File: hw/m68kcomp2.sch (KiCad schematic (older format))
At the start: 1 part

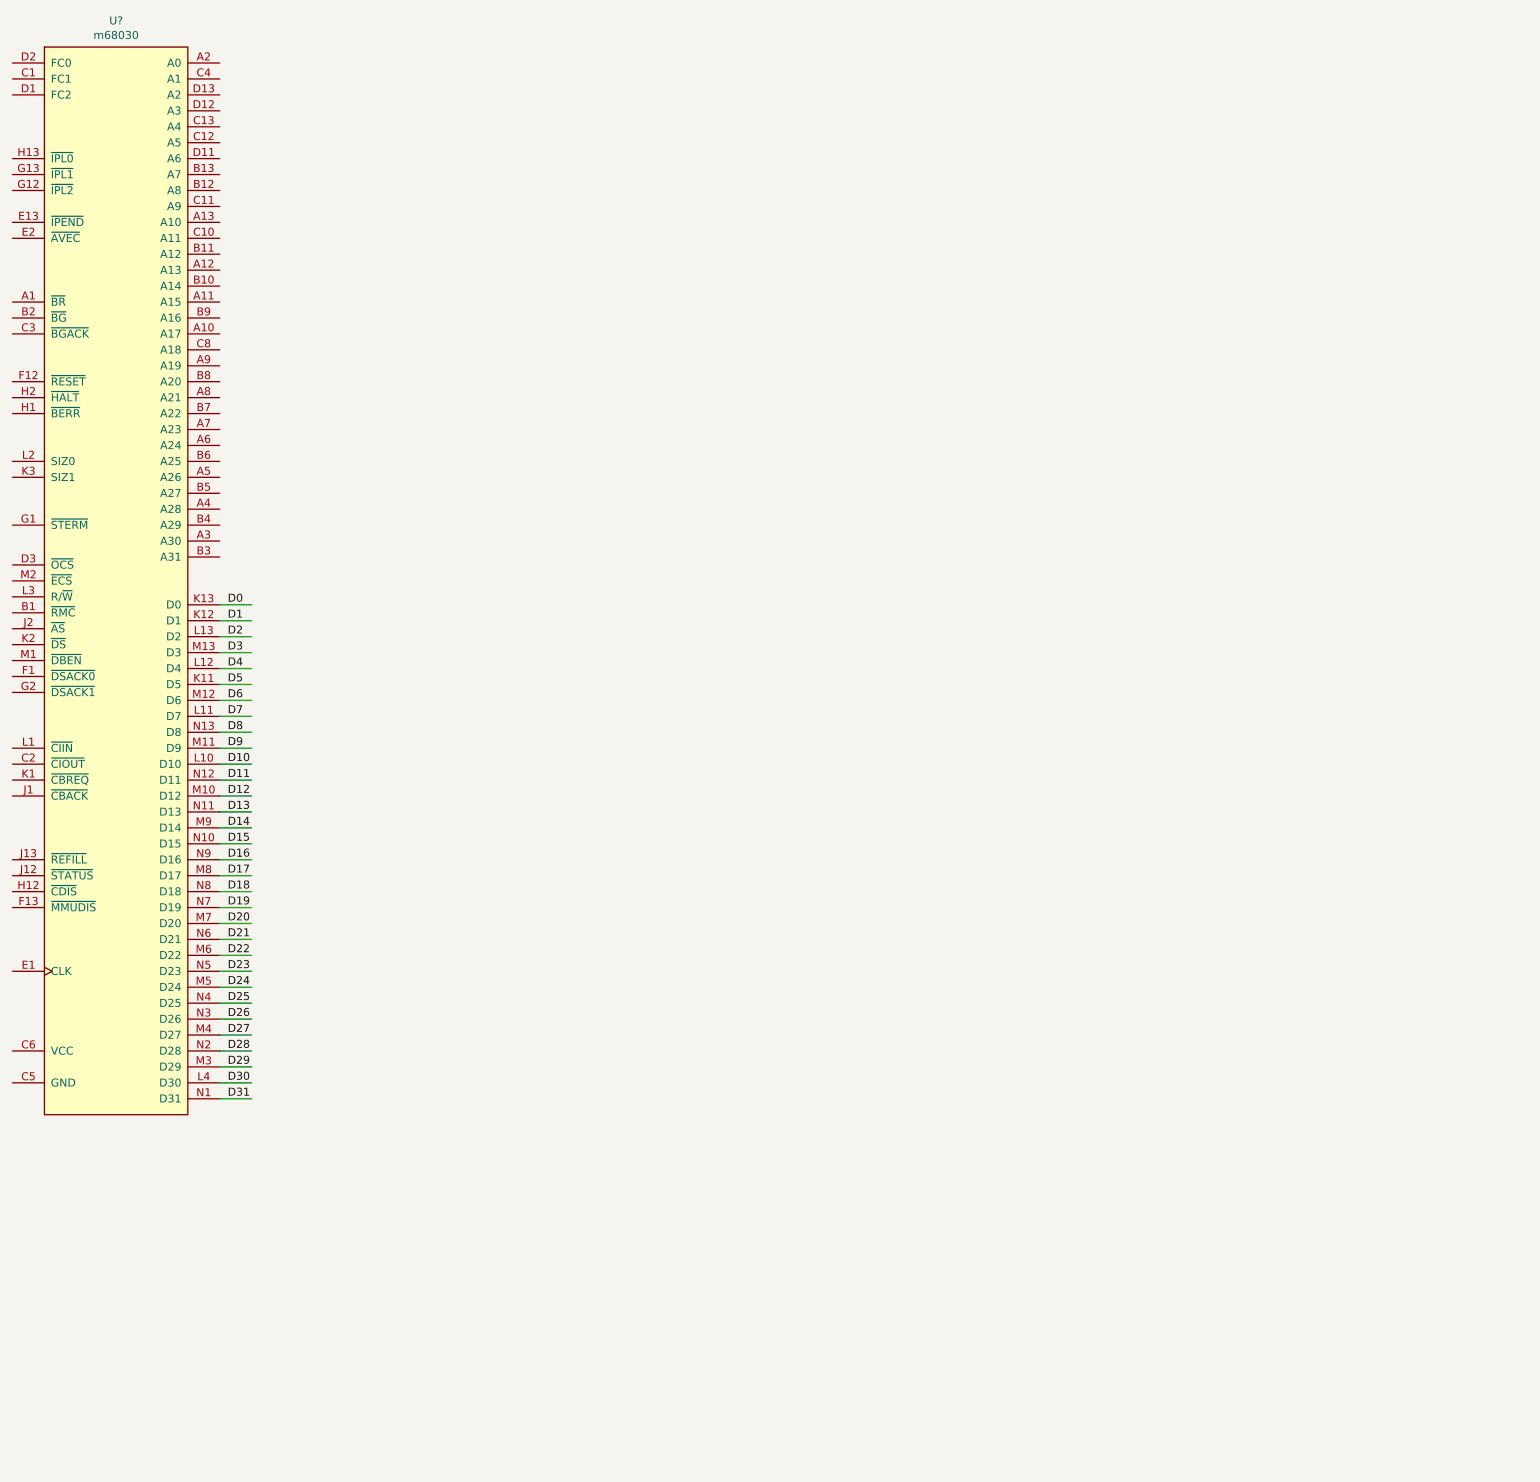
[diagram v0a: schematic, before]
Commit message: finished the 68881 symbol, and added a few major components on a schematic sheet
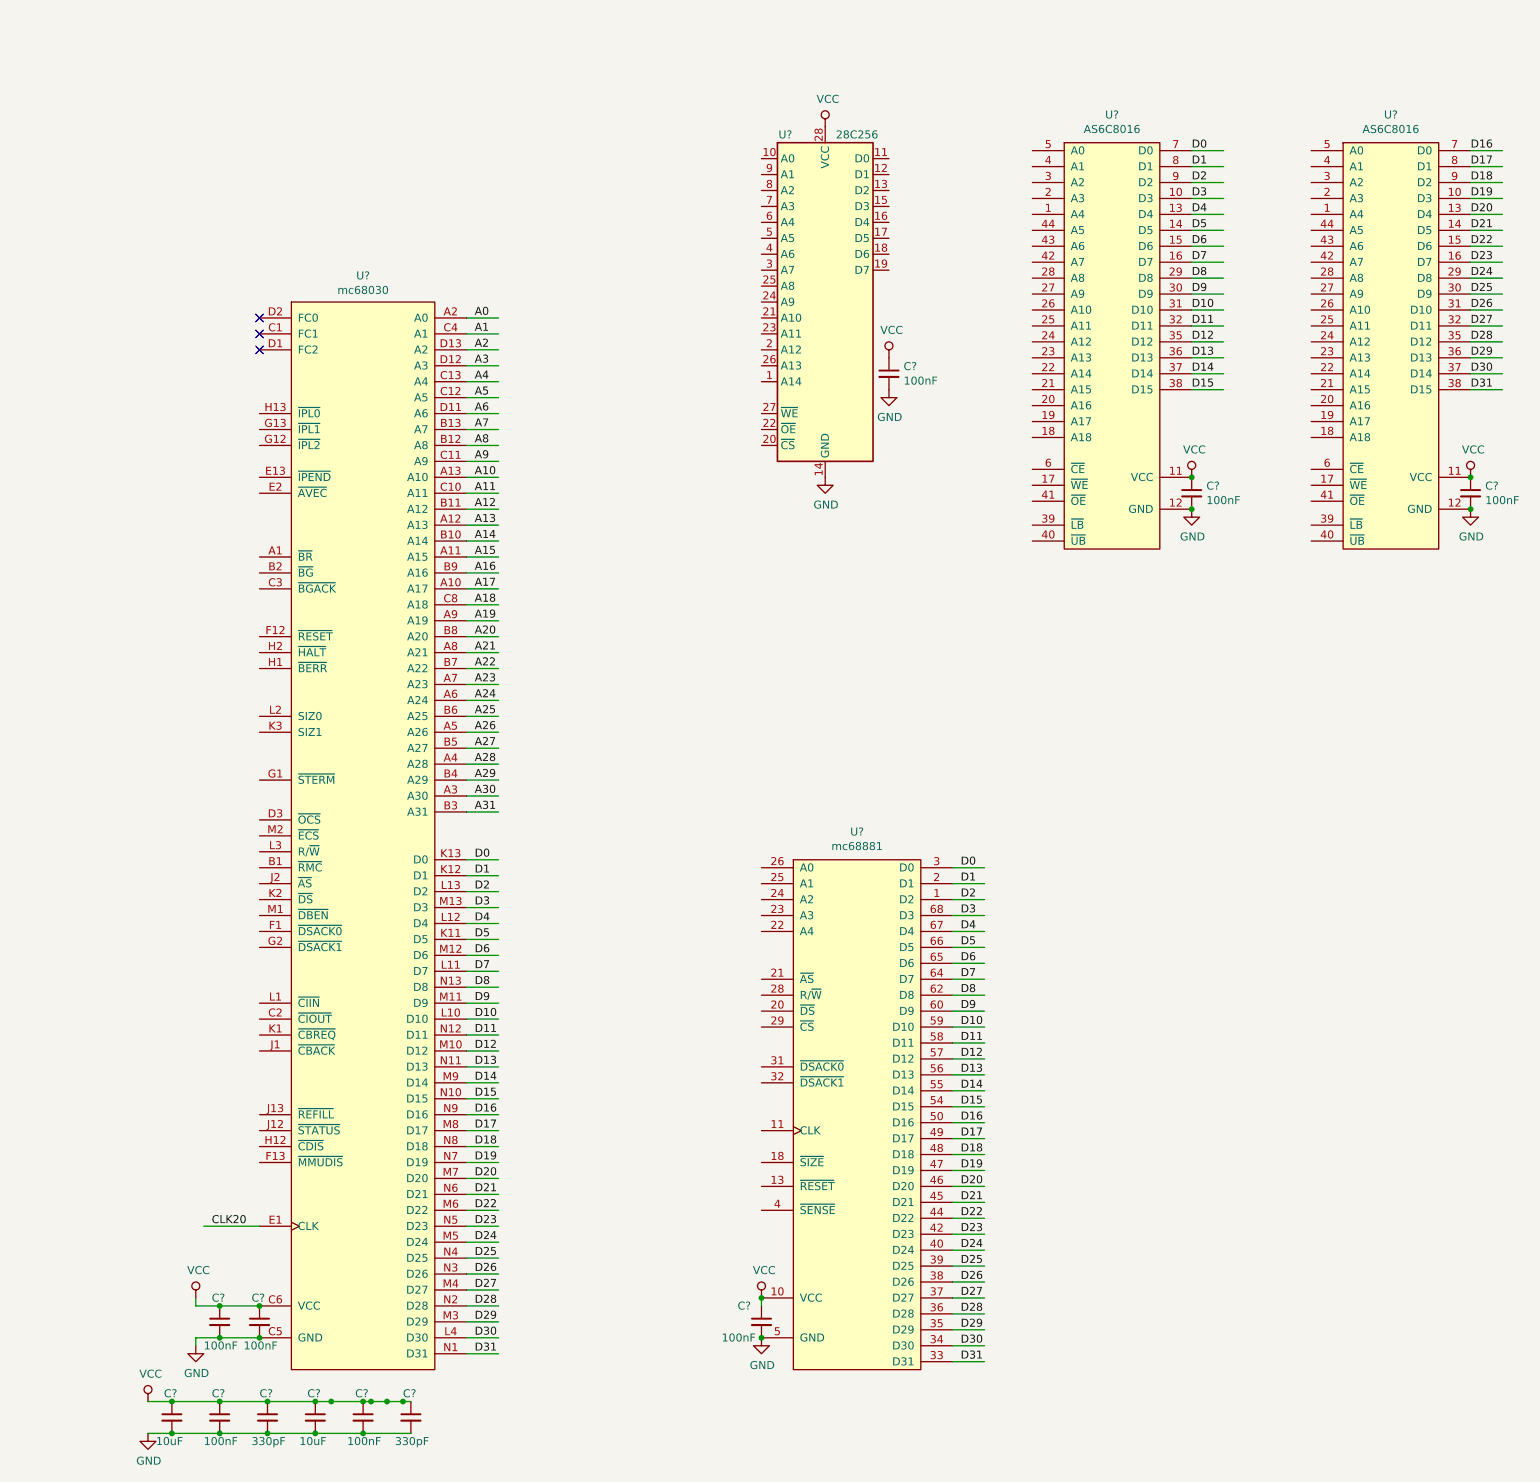
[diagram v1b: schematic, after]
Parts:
- removed U?: m68030, symbol m68kcomp2:m68030
- added C? (x8): 100nF, symbol Device:C_Small
- added C? (x2): 330pF, symbol Device:C_Small
- added C? (x2): 10uF, symbol Device:C_Small
- added U?: mc68030, symbol m68kcomp2:mc68030
- added U? (x2): AS6C8016, symbol m68kcomp2:AS6C8016
- added U?: 28C256, symbol Memory_EEPROM:28C256
- added U?: mc68881, symbol m68kcomp2:mc68881
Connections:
- net labels added: A0, A1, A10, A11, A12, A13, A14, A15, A16, A17, A18, A19, A2, A20, A21, A22, A23, A24, A25, A26, A27, A28, A29, A3, A30, A31, A4, A5, A6, A7, A8, A9, CLK20, GND, VCC
- wire segments 32 -> 152
- no-connect marks 0 -> 3
